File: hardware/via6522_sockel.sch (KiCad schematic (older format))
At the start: 3 parts, among them P3 VIA_PIN_1-20, P4 DIL40, P5 VIA_PIN_21-40

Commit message: Sourcecode neu überarbeitet, Schaltplan angepasst und DOC bearbeitet
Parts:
- added U1: 74LS244, symbol 74LS244
- renumbered P3 to P1, P4 to P2, P5 to P3
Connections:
- net labels added: D0, D1, D2, D3, D4, D5, D6, D7
- wire segments 56 -> 76
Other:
- moved on the sheet: P1, P2, P3

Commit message: Schaltplan angepasst und Firmware angepasst
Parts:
- removed U1: 74LS244, symbol 74LS244
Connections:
- net labels removed: D0, D1, D2, D3, D4, D5, D6, D7
- wire segments 76 -> 57
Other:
- moved on the sheet: P1, P2, P3

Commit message: WPS Signal zum Diskwechsel anzeigen eingebaut. Laden des Track18 eines ausgewählten G64. Schaltpaln aktuallisiert
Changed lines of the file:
@@
 Wire Wire Line
 	3950 2400 3950 3200
+Text HLabel 5250 2650 1    60   Input ~ 0
+WPS
+Wire Wire Line
+	5250 2650 5250 4200
+Connection ~ 5250 4200
 $EndSCHEMATC

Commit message: diverese Sachen geändert
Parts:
- P2: renamed from P1; footprint pin_header:pin_header_1x20_smd -> Pin_Headers:Pin_Header_Straight_1x20
- P4: renamed from P3; footprint pin_header:pin_header_1x20_smd -> Pin_Headers:Pin_Header_Straight_1x20
- renumbered P2 to P3
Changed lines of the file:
@@
 $EndDescr
 $Comp
-L DIL40 P2
+L DIL40 P3
 U 1 1 55F9CFCC
 P 6400 3850
-F 0 "P2" H 6400 4900 70  0000 C CNN
+F 0 "P3" H 6400 4900 70  0000 C CNN
 F 1 "DIL40" V 6400 3850 60  0000 C CNN
 F 2 "Housings_DIP:DIP-40_W15.24mm_LongPads" H 6400 3850 60  0001 C CNN
@@
 $EndComp
 $Comp
-L CONN_01X20 P3
+L CONN_01X20 P4
 U 1 1 55F9DAC3
 P 8700 3850
-F 0 "P3" H 8700 4900 50  0000 C CNN
+F 0 "P4" H 8700 4900 50  0000 C CNN
 F 1 "VIA_PIN_21-40" V 8800 3850 50  0000 C CNN
-F 2 "pin_header:pin_header_1x20_smd" H 8700 3850 60  0001 C CNN
+F 2 "Pin_Headers:Pin_Header_Straight_1x20" H 8700 3850 60  0001 C CNN
 F 3 "" H 8700 3850 60  0000 C CNN
 	1    8700 3850
@@
 $EndComp
 $Comp
-L CONN_01X20 P1
+L CONN_01X20 P2
 U 1 1 55F9DB72
 P 3100 3850
-F 0 "P1" H 3100 4900 50  0000 C CNN
+F 0 "P2" H 3100 4900 50  0000 C CNN
 F 1 "VIA_PIN_1-20" V 3200 3850 50  0000 C CNN
-F 2 "pin_header:pin_header_1x20_smd" H 3100 3850 60  0001 C CNN
+F 2 "Pin_Headers:Pin_Header_Straight_1x20" H 3100 3850 60  0001 C CNN
 F 3 "" H 3100 3850 60  0000 C CNN
 	1    3100 3850
@@
 BRDY
 $Comp
-L GND #PWR016
+L GND #PWR019
 U 1 1 55F9667E
 P 6000 2650
-F 0 "#PWR016" H 6000 2400 50  0001 C CNN
+F 0 "#PWR019" H 6000 2400 50  0001 C CNN
 F 1 "GND" H 6000 2500 50  0000 C CNN
 F 2 "" H 6000 2650 60  0000 C CNN
@@
 $EndComp
 $Comp
-L +5V #PWR017
+L +5V #PWR020
 U 1 1 55F96755
 P 6000 5000
-F 0 "#PWR017" H 6000 4850 50  0001 C CNN
+F 0 "#PWR020" H 6000 4850 50  0001 C CNN
 F 1 "+5V" H 6000 5140 50  0000 C CNN
 F 2 "" H 6000 5000 60  0000 C CNN

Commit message: Platine per Autorouter geroutet.
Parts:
- P3: footprint Housings_DIP:DIP-40_W15.24mm_LongPads -> w_pth_circuits:dil_40-600_socket
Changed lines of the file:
@@
 LIBS:valves
 LIBS:Oscillators
+LIBS:w_analog
+LIBS:w_connectors
+LIBS:w_device
+LIBS:w_logic
+LIBS:w_memory
+LIBS:w_microcontrollers
+LIBS:w_opto
+LIBS:w_relay
+LIBS:w_rtx
+LIBS:w_transistor
+LIBS:w_vacuum
 LIBS:1541-rebuild-cache
 EELAYER 25 0
@@
 F 0 "P3" H 6400 4900 70  0000 C CNN
 F 1 "DIL40" V 6400 3850 60  0000 C CNN
-F 2 "Housings_DIP:DIP-40_W15.24mm_LongPads" H 6400 3850 60  0001 C CNN
+F 2 "w_pth_circuits:dil_40-600_socket" H 6400 3850 60  0001 C CNN
 F 3 "" H 6400 3850 60  0000 C CNN
 	1    6400 3850

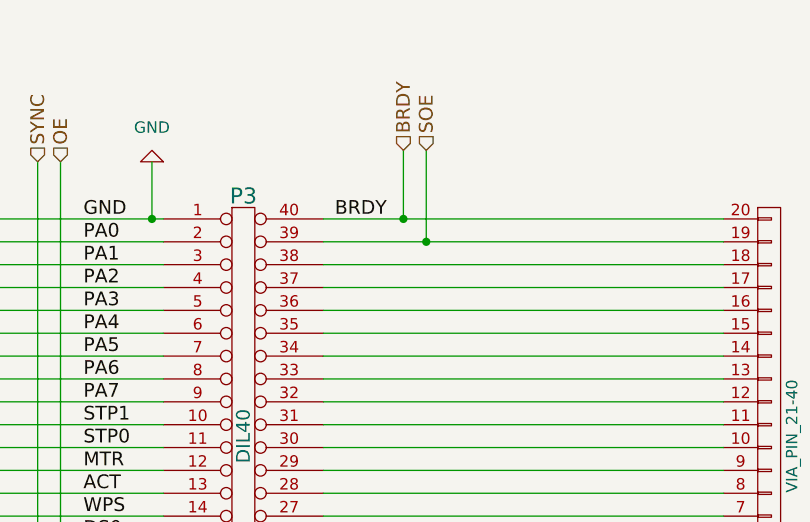
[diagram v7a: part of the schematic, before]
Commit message: Schaltplan angepasst. Reset kann optional per Jumper zwischen uController und Floppy Elektronik verbunden werden. Somit wird die Adapterplatine resettet wenn der C64 neu gestartet wird.
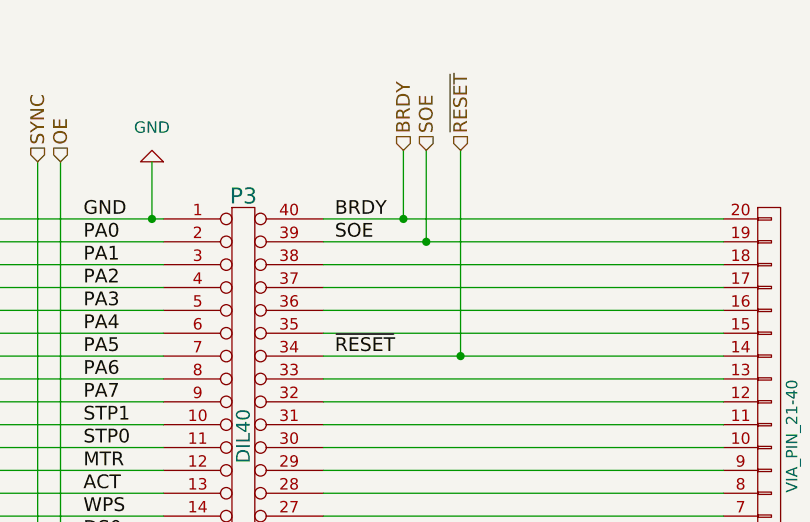
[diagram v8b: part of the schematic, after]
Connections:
- net ~RESET: now reaches P3.34, P4.14 (P14)
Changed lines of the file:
@@
 	5250 2650 5250 4200
 Connection ~ 5250 4200
+Text HLabel 7350 2600 1    60   Input ~ 0
+~RESET
+Wire Wire Line
+	7350 2600 7350 3500
+Connection ~ 7350 3500
+Text Label 6800 3000 0    60   ~ 0
+SOE
+Text Label 6800 3500 0    60   ~ 0
+~RESET
 $EndSCHEMATC
